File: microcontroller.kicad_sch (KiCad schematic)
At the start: 41 parts, among them J5 USB4105-GF-A, J7 DEBUG, U2 W25Q32JV, U3 RP2350A, U4 MCP1702T-3302E_CB, X1 IQXO-791

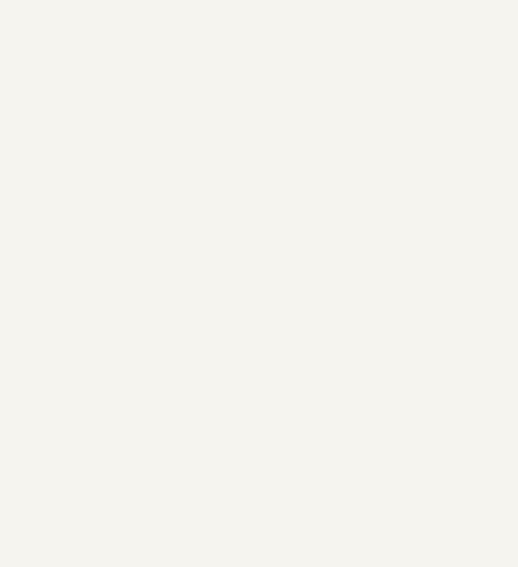
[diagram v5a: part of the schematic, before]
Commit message: Begin positioning and grouping components
Add bypass caps to level shifters Vdd
Rearrange pins on shift register
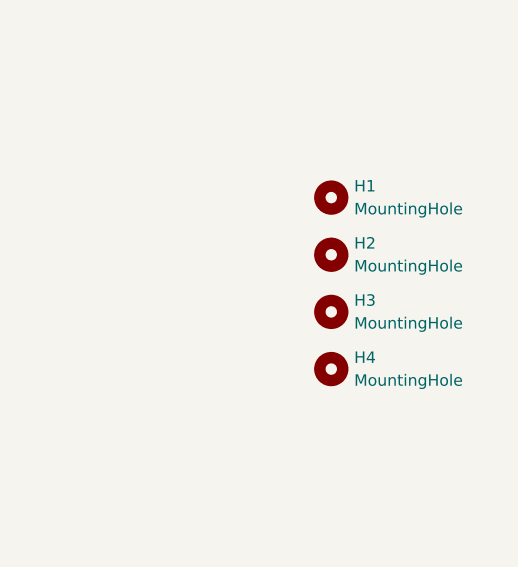
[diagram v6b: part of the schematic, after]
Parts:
- added H1, H2, H3, H4: MountingHole, MountingHole:MountingHole_3.2mm_M3, symbol Mechanical:MountingHole

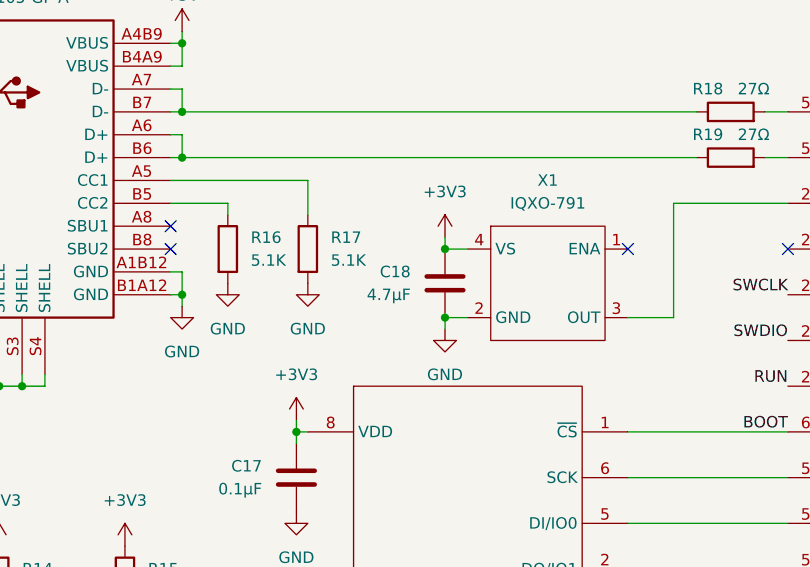
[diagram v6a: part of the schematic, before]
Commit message: Add DigiKey part numbers to components
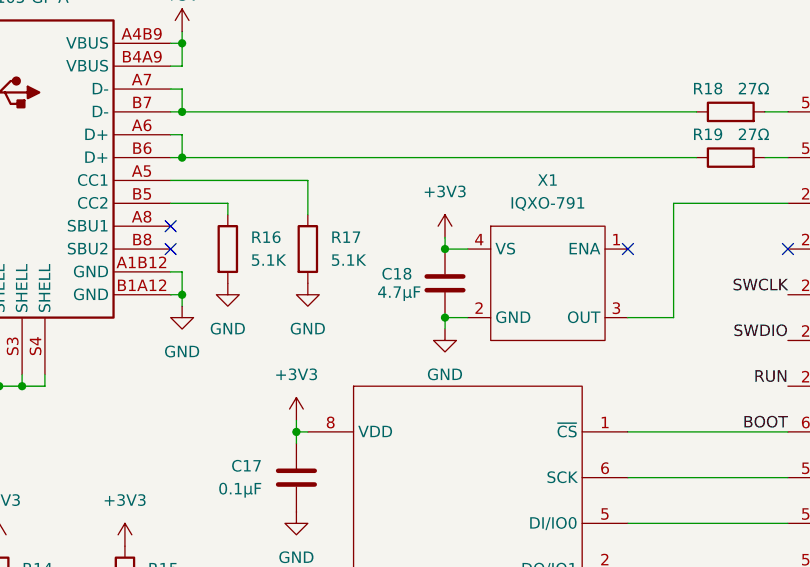
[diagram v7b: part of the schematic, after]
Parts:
- C17, C20, C21, C22, C23, C24, C25, C26, C29, C31: DigikeyPN (none) -> 1276-1033-1-ND
- C18, C19, C27, C28, C30: DigikeyPN (none) -> 490-GRM188Z71C475KE21DCT-ND
- C32, C33: DigikeyPN (none) -> 490-18214-1-ND
- D3: DigikeyPN (none) -> 1497-XZCM2MOK54WA-1VFCT-ND
- D4: DigikeyPN (none) -> 1830-1086-1-ND
- D5: DigikeyPN (none) -> 160-1887-1-ND
- J5: DigikeyPN (none) -> 2073-USB4105-GF-ACT-ND
- R14, R15, R16, R17, R22: DigikeyPN (none) -> P5.10KHCT-ND
- R18, R19: DigikeyPN (none) -> 311-27.0HRCT-ND
- R20: DigikeyPN (none) -> 13-RC0603FR-0733RLCT-ND
- R21, R23, R24, R25: DigikeyPN (none) -> 311-1.00KHRCT-ND
- S1, S2: DigikeyPN (none) -> SW1020CT-ND
- U2: DigikeyPN (none) -> W25Q32JVZPIQ TR
- U3: DigikeyPN (none) -> 2648-SC1509-A4CT-ND

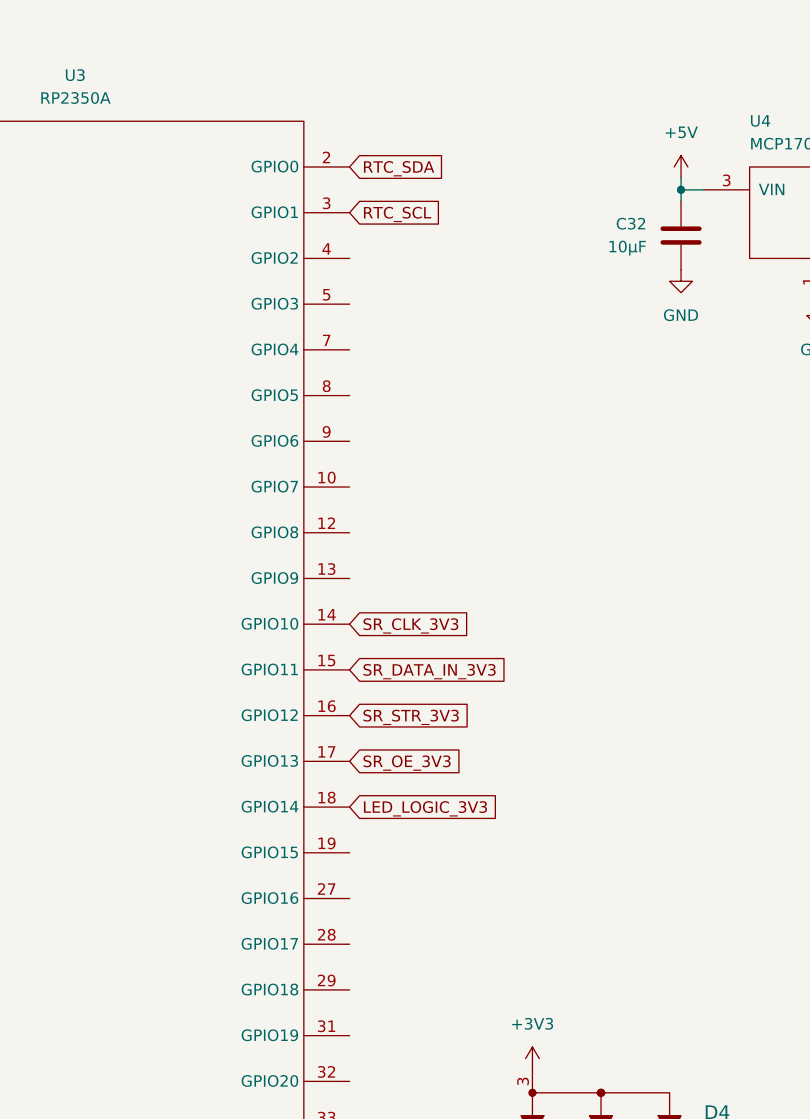
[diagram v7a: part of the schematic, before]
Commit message: Begin layout of microcontroller components
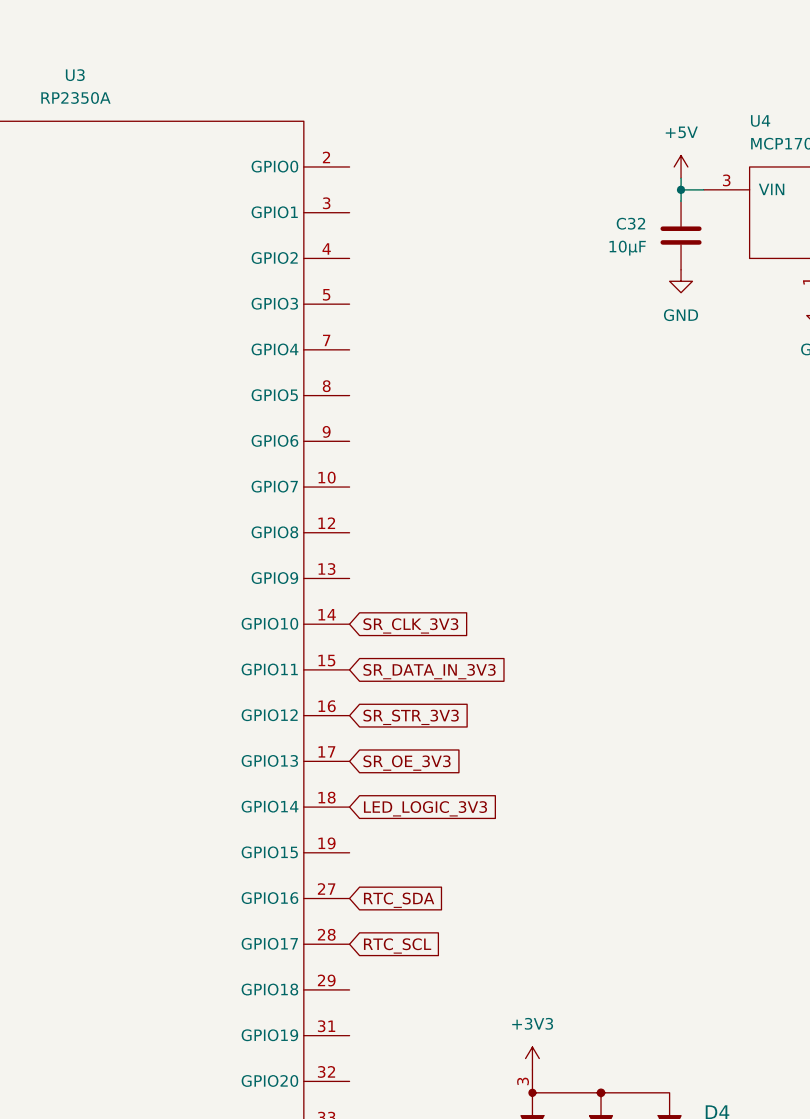
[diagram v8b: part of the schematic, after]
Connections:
- net RTC_SCL: now also U3.28 (GPIO17); no longer U3.3 (GPIO1)
- net RTC_SDA: now also U3.27 (GPIO16); no longer U3.2 (GPIO0)
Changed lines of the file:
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@@
-		)
-	)
-	(global_label "RTC_SCL"
-		(shape input)
-		(at 167.64 31.75 0)
-		(fields_autoplaced yes)
-		(effects
-			(font
-				(size 1.27 1.27)
-			)
-			(justify left)
-		)
-		(property "Intersheetrefs" "${INTERSHEET_REFS}"
-			(at 178.608 31.75 0)
-			(effects
-				(font
-					(size 1.27 1.27)
-				)
-				(justify left)
-				(hide yes)
-			)
 		)
 	)
@@
 		)
 	)
+	(global_label "RTC_SDA"
+		(shape input)
+		(at 167.64 107.95 0)
+		(fields_autoplaced yes)
+		(effects
+			(font
+				(size 1.27 1.27)
+			)
+			(justify left)
+		)
+		(property "Intersheetrefs" "${INTERSHEET_REFS}"
+			(at 178.6685 107.95 0)
+			(effects
+				(font
+					(size 1.27 1.27)
+				)
+				(justify left)
+				(hide yes)
+			)
+		)
+	)
 	(global_label "SR_STR_3V3"
 		(shape input)
@@
 		(property "Intersheetrefs" "${INTERSHEET_REFS}"
 			(at 181.9946 87.63 0)
-			(effects
-				(font
-					(size 1.27 1.27)
-				)
-				(justify left)
-				(hide yes)
-			)
-		)
-	)
-	(global_label "RTC_SDA"
-		(shape input)
-		(at 167.64 26.67 0)
-		(fields_autoplaced yes)
-		(effects
-			(font
-				(size 1.27 1.27)
-			)
-			(justify left)
-		)
-		(property "Intersheetrefs" "${INTERSHEET_REFS}"
-			(at 178.6685 26.67 0)
 			(effects
 				(font
@@
 			(effects
 				(font
+					(size 1.27 1.27)
+				)
+				(justify left)
+				(hide yes)
+			)
+		)
+	)
+	(global_label "RTC_SCL"
+		(shape input)
+		(at 167.64 113.03 0)
+		(fields_autoplaced yes)
+		(effects
+			(font
+				(size 1.27 1.27)
+			)
+			(justify left)
+		)
+		(property "Intersheetrefs" "${INTERSHEET_REFS}"
+			(at 178.608 113.03 0)
+			(effects
+				(font
